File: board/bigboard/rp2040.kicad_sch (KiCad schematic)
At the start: 24 parts, among them J5 Conn_01x03_Male, J6 Conn_01x03_Male, J7 Conn_01x03_Male, SW1 SW_Push, U4 RP2040, Y1 12MHz

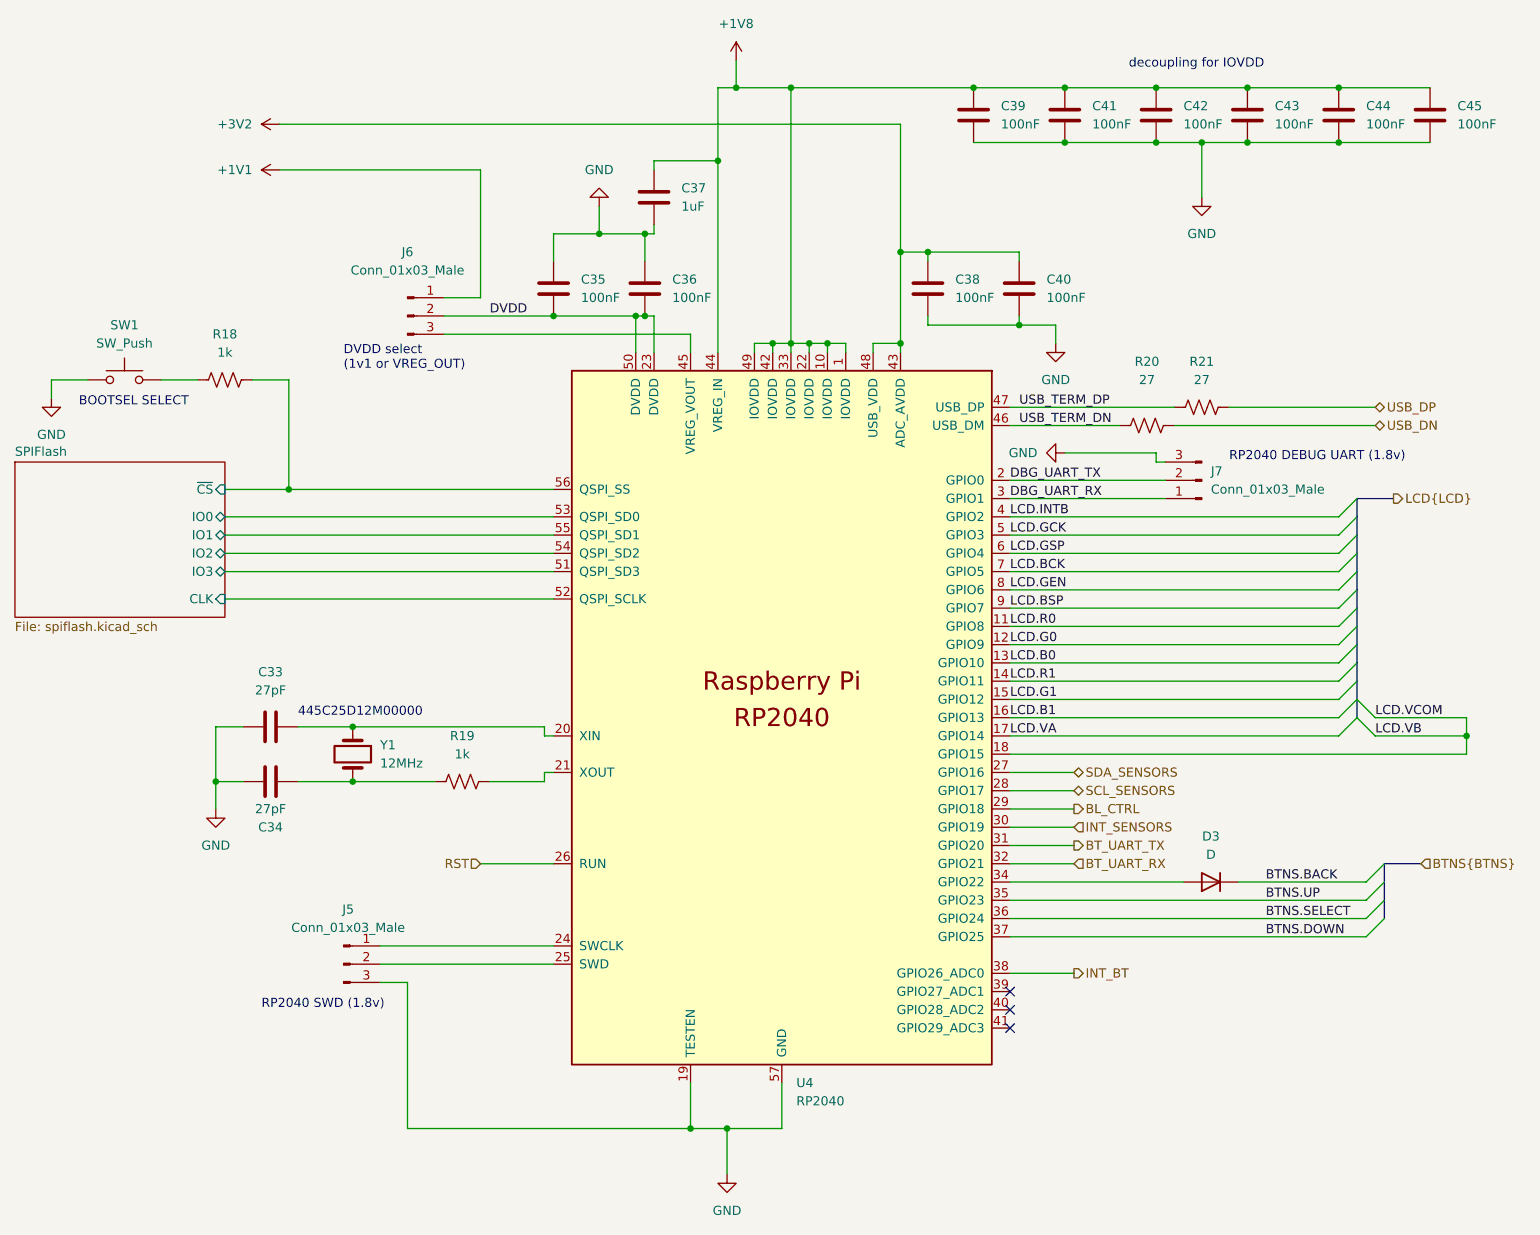
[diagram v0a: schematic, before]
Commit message: Manufactured version of bigboard
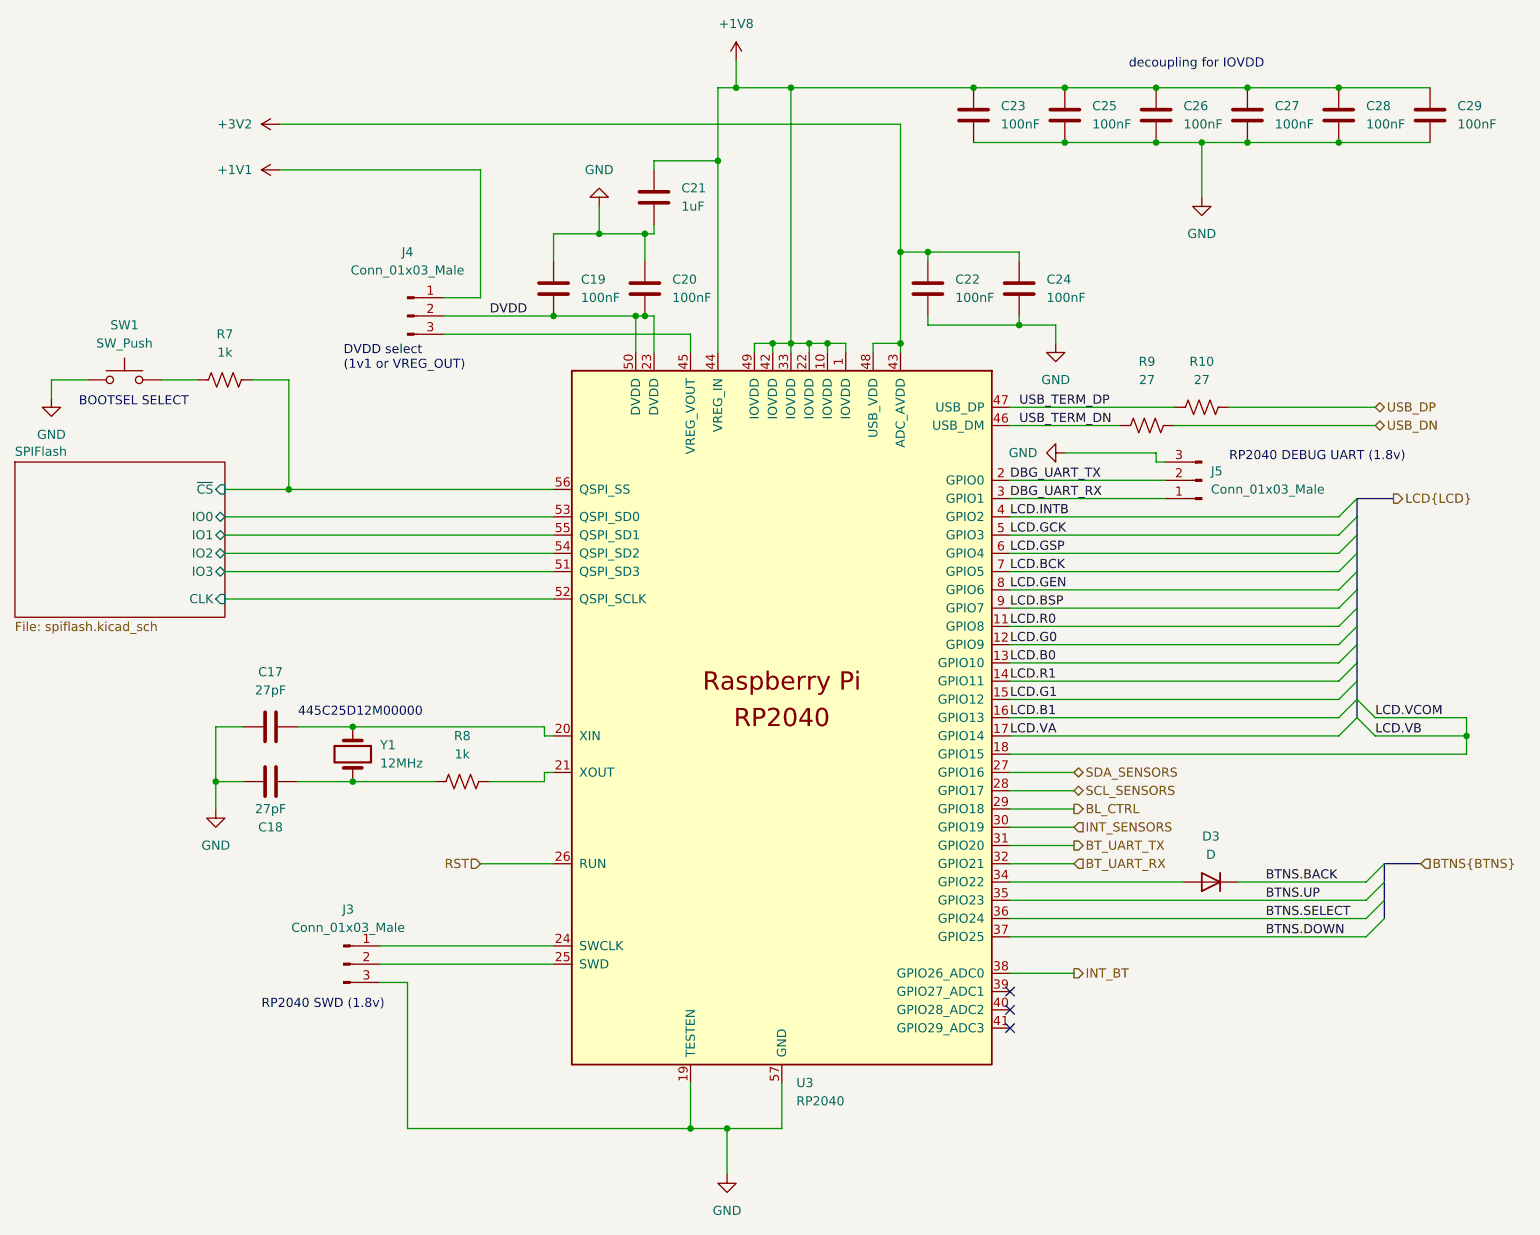
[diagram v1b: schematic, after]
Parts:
- C17: renamed from C33; MPN (none) -> CC0201JRNPO9BN270
- C18: renamed from C34; MPN (none) -> CC0201JRNPO9BN270
- C19: renamed from C35; MPN (none) -> CC0201KRX5R8BB104
- C20: renamed from C36; MPN (none) -> CC0201KRX5R8BB104
- C21: renamed from C37; MPN (none) -> CC0201MRX5R6BB105
- C22: renamed from C38; MPN (none) -> CC0201KRX5R8BB104
- C23: renamed from C39; MPN (none) -> CC0201KRX5R8BB104
- C24: renamed from C40; MPN (none) -> CC0201KRX5R8BB104
- C25: renamed from C41; MPN (none) -> CC0201KRX5R8BB104
- C26: renamed from C42; MPN (none) -> CC0201KRX5R8BB104
- C27: renamed from C43; MPN (none) -> CC0201KRX5R8BB104
- C28: renamed from C44; MPN (none) -> CC0201KRX5R8BB104
- C29: renamed from C45; MPN (none) -> CC0201KRX5R8BB104
- R10: renamed from R21; MPN (none) -> RC0201FR-0727RL
- R7: renamed from R18; MPN (none) -> RC0201FR-071KL
- R8: renamed from R19; MPN (none) -> RC0201FR-071KL
- R9: renamed from R20; MPN (none) -> RC0201FR-0727RL
- renumbered J5 to J3, J6 to J4, J7 to J5, U4 to U3

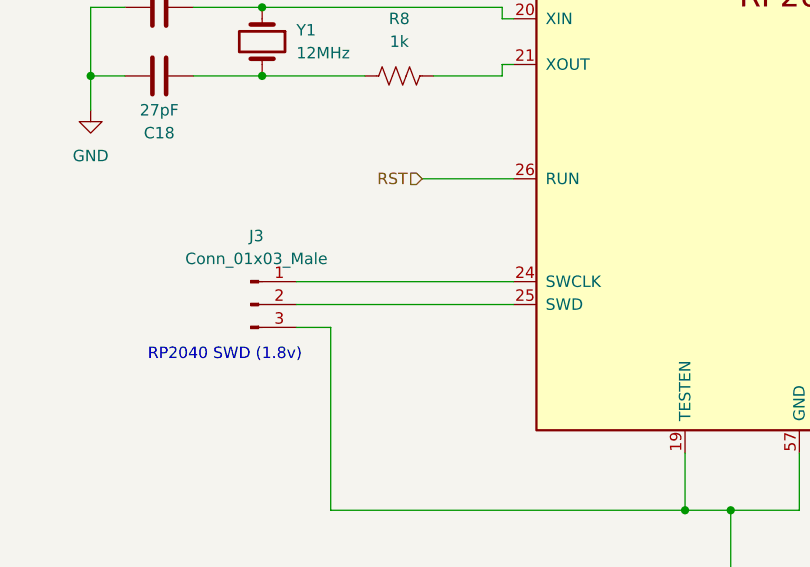
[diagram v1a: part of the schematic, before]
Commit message: Update board to kicad 7
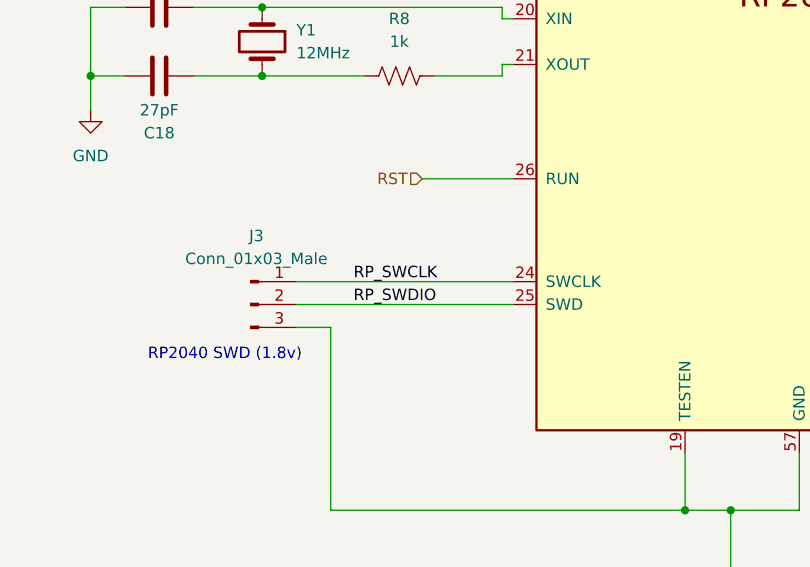
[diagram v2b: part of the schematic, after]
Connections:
- net RP_SWCLK: now reaches J3.1 (Pin_1), U3.24 (SWCLK)
- net RP_SWDIO: now reaches J3.2 (Pin_2), U3.25 (SWD)
